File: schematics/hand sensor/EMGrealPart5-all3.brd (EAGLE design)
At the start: 88.9 x 154.9 mm, 145 parts, among them IC1 INA118P, IC10 INA118P, IC11 OP275P, IC12 OP275P, IC13 MCP3208c, IC14 MCP3208c, IC2 OP275P, IC3 OP275P, IC4 INA118P, IC5 OP275P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

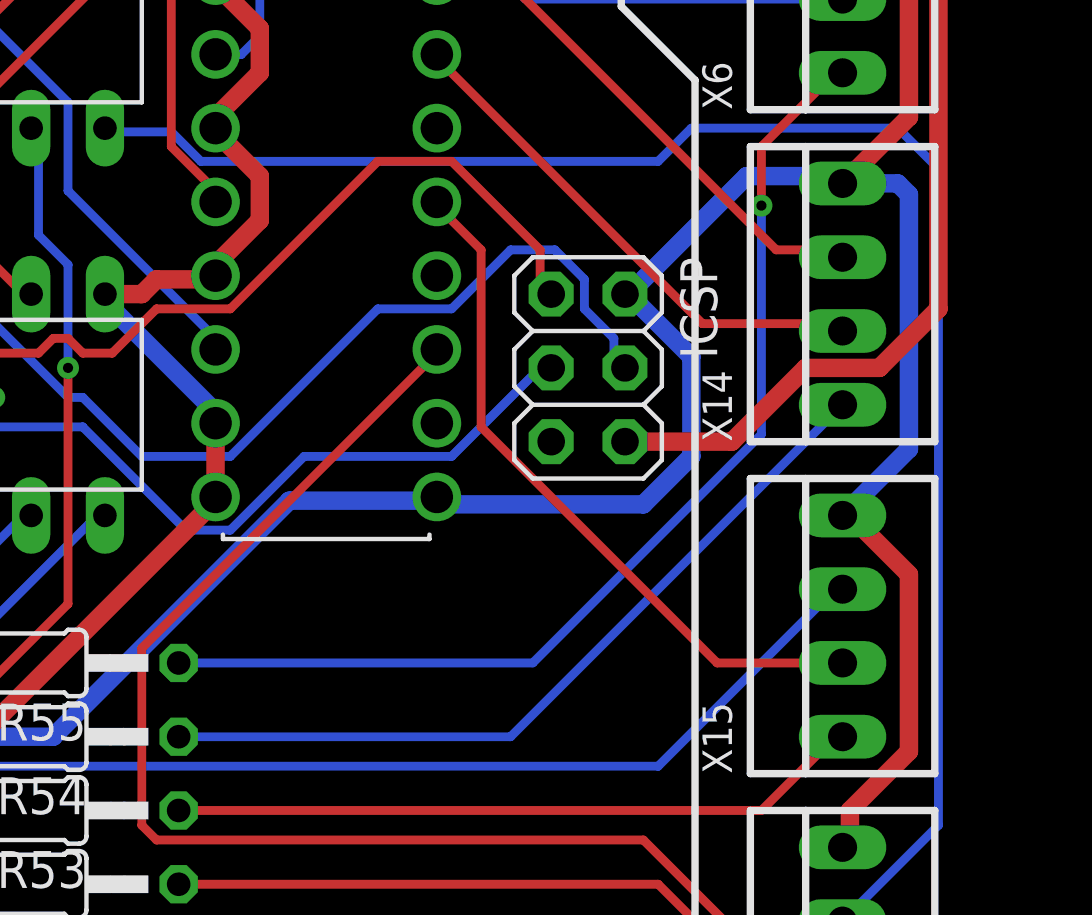
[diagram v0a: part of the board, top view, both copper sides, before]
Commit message: Implement socket transfering
Implement socket transfering between Python and Unity.
Arduino now has IR sensor implemented.
Record 10 signal from sensor (before fix).
Implement and train several models.
Implement data analytic module.
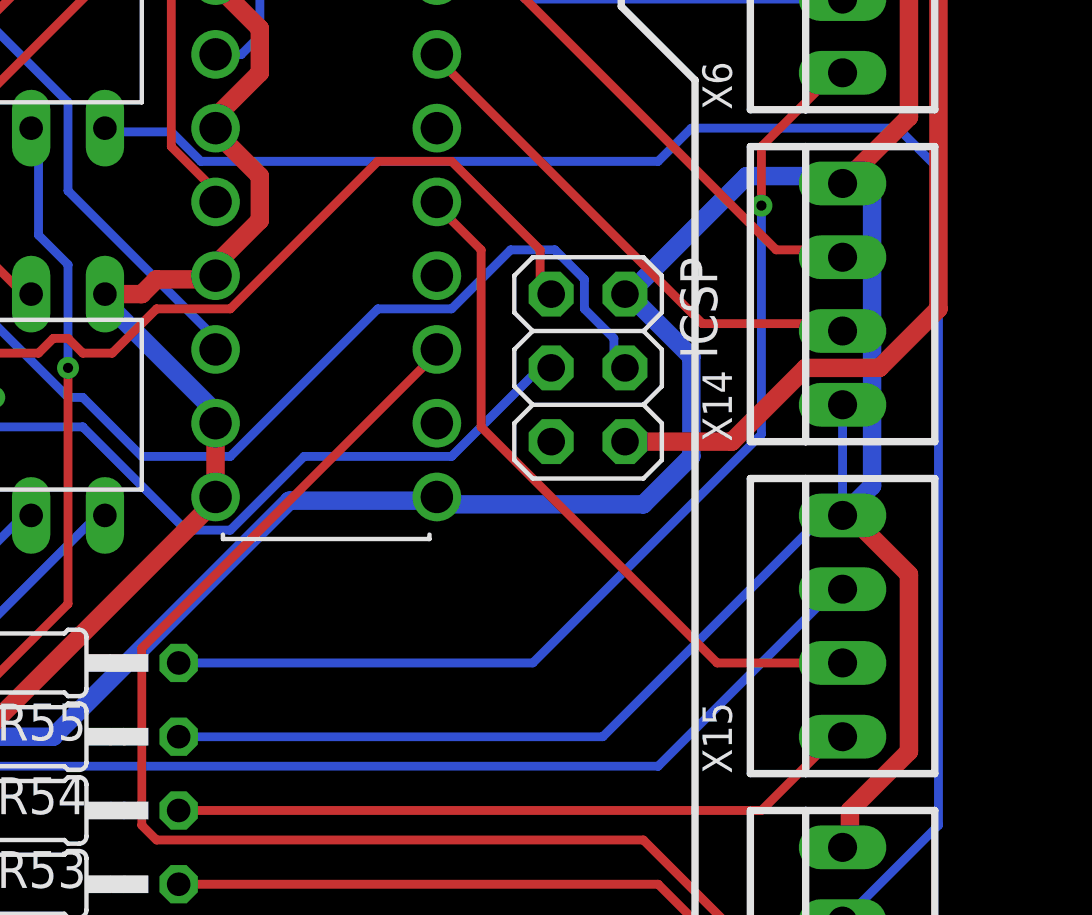
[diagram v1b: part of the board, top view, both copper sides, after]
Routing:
- net N$99: track 27.6 -> 29.5 mm
- net +5V: track 257.5 -> 255.9 mm
